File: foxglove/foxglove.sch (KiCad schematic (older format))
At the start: 50 parts, among them J1 NEIGHBOR1, J2 NEIGHBOR2, J3 Conn_02x05_Odd_Even, J4 Conn_02x05_Odd_Even, J5 Conn_01x02_Female, J7 BONUS_ROW, U1 ICE40HX8K-CT256, U2 TLV711, U3 MC4558CPT, U4 74LVC1G3157, U5 LM339, U6 ADP225, U7 DAC084S085, U8 74AHC1G04

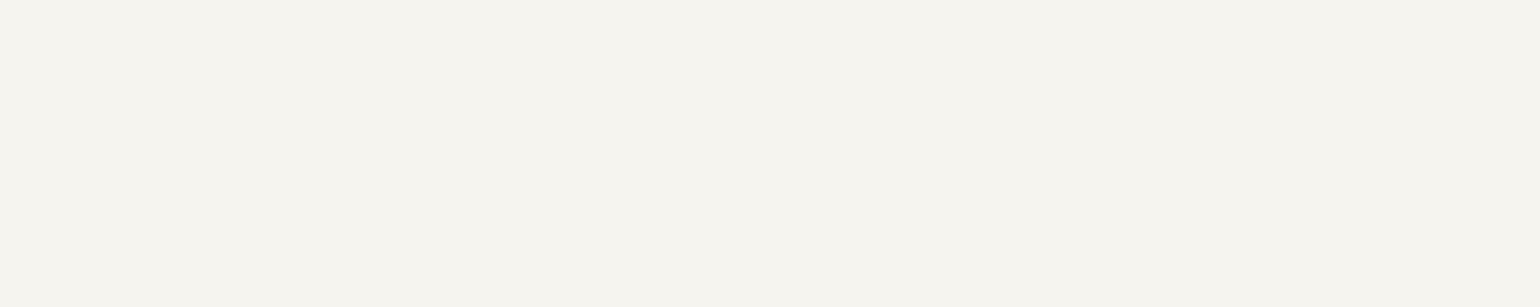
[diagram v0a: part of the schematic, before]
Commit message: Added LFE5U-12F-6BG256C to schematic
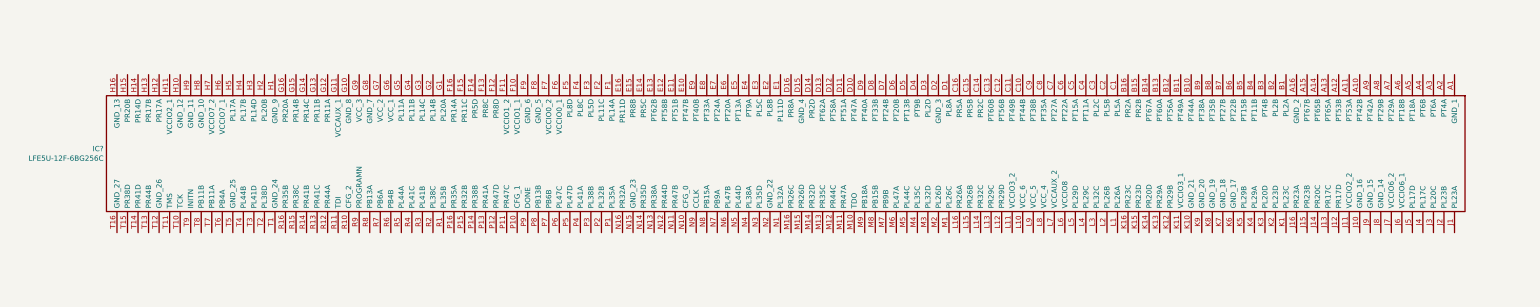
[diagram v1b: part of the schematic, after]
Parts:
- added IC?: LFE5U-12F-6BG256C, BGA256C80P16X16_1400X1400X170, symbol gsg-symbols:LFE5U-12F-6BG256C
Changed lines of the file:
@@
 Text Notes 15900 8150 0    50   ~ 0
 use LDO like \nhttps://www.diodes.com/assets/Datasheets/AP2127.pdf\ninstead
+Text Notes 11600 4200 0    50   ~ 0
+need to compare between pins?
 Wire Bus Line
 	2600 1900 4600 1900
@@
 Wire Bus Line
 	3150 6800 6450 6800
-Text Notes 11600 4200 0    50   ~ 0
-need to compare between pins?
+$Comp
+L gsg-symbols:LFE5U-12F-6BG256C IC?
+U 1 1 5CBE08F5
+P -1600 5850
+F 0 "IC?" V -896 -6977 50  0000 R CNN
+F 1 "LFE5U-12F-6BG256C" V -805 -6977 50  0000 R CNN
+F 2 "BGA256C80P16X16_1400X1400X170" H -250 5950 50  0001 L CNN
+F 3 "http://www.latticesemi.com/~/media/LatticeSemi/Documents/DataSheets/ECP5/FPGA-DS-02012.pdf?document_id=50461" H -250 5850 50  0001 L CNN
+F 4 "FPGA - Field Programmable Gate Array ECP5; 12k LUTs; 1.1V" H -250 5750 50  0001 L CNN "Description"
+F 5 "1.7" H -250 5650 50  0001 L CNN "Height"
+F 6 "Lattice" H -250 5550 50  0001 L CNN "Manufacturer_Name"
+F 7 "LFE5U-12F-6BG256C" H -250 5450 50  0001 L CNN "Manufacturer_Part_Number"
+F 8 "842-LFE5U12F6BG256C" H -250 5350 50  0001 L CNN "Mouser Part Number"
+F 9 "https://www.mouser.com/Search/Refine.aspx?Keyword=842-LFE5U12F6BG256C" H -250 5250 50  0001 L CNN "Mouser Price/Stock"
+	1    -1600 5850
+	0    1    1    0
+$EndComp
 $EndSCHEMATC

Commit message: Routed FPGA power and JTAG connections
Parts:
- removed U2: TLV711, Package_SON:WSON-6_1.5x1.5mm_P0.5mm, symbol gsg-symbols:TLV711
- added R41: 25k, gsg-modules:0402, symbol Device:R
- added R42, R43: 100k, gsg-modules:0402, symbol Device:R
- added R44: 120k, gsg-modules:0402, symbol Device:R
- added R45: 10k, gsg-modules:0402, symbol Device:R
- added R46, R47: R, gsg-modules:0402, symbol Device:R
- added R? (x4): 4.7k, gsg-modules:0402, symbol Device:R
- added U2: ADP225, Package_CSP:LFCSP-8_2x2mm_P0.5mm, symbol gsg-symbols:ADP225
- added U25: 74LVC1G53, symbol gsg-symbols:74LVC1G53
- IC1: renamed from IC?; footprint BGA256C80P16X16_1400X1400X170 -> gsg-modules:BGA256C80P16X16_1400X1400X170
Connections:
- net labels added: +1V1, ADC_pull, EN_pull, TCK, TDI, TDO, TMS
- wire segments 323 -> 415
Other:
- note removed: "keep separate direction signals"
- moved on the sheet: C8, U5

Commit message: Made FPGA connections to greatfet headers
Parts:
- added J?: Conn_02x03_Odd_Even, symbol Connector_Generic:Conn_02x03_Odd_Even
- added R? (x6): 4.7k, gsg-modules:0402, symbol Device:R
- added R?: 1k, gsg-modules:0402, symbol Device:R
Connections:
- net labels added: CCLK, CFG_0, CFG_1, CFG_2, CSSPIN, INITN, J7.02, J7.03, J7.04, J7.05, J7.06, J7.07, J7.08, J7.09, J7.10, J7.11, J7.12, J7.13, J7.14, J7.15, J7.16, J7.17, J7.18, PROGRAMN
- wire segments 415 -> 462
- no-connect marks 21 -> 1
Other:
- note added: "Do we want all banks \nto be at VCCI0x = 3.3V?"
- note added: "JTAG"
- note added: "check ordering of CFG pins\nfor default setup\nSSPI: CFG[2:0] = 001"
- note removed: "make FPGA connections \nto bonus row?"
- moved on the sheet: J1, J2, J3, J4, J7, R?

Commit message: Started routing connections to J2 and J7
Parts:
- removed C1, C3: 10uF, gsg-modules:0402, symbol Device:C
- removed C2, C4: 100nF, gsg-modules:0402, symbol Device:C
- removed R1, R4, R5: 10k, gsg-modules:0402, symbol Device:R
- removed R2: ???, gsg-modules:0402, symbol Device:R
- removed R3, R6: 100, gsg-modules:0402, symbol Device:R
- removed U1: ICE40HX8K-CT256, gsg-modules:BGA256C80P16X16_1400X1400X170, symbol gsg-symbols:ICE40HX8K-CT256
- J6: renamed from J?; footprint (none) -> gsg-modules:HEADER-2x3
- U25: footprint (none) -> Package_SO:VSSOP-8_2.3x2mm_P0.5mm
- gave numbers to parts that had none: 11
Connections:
- net labels removed: +1V2, CCLK, CDONE, CRESET
- wire segments 462 -> 349
- no-connect marks 1 -> 0
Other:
- moved on the sheet: C5, C6, C7, R41, R42, R43, R44, U2

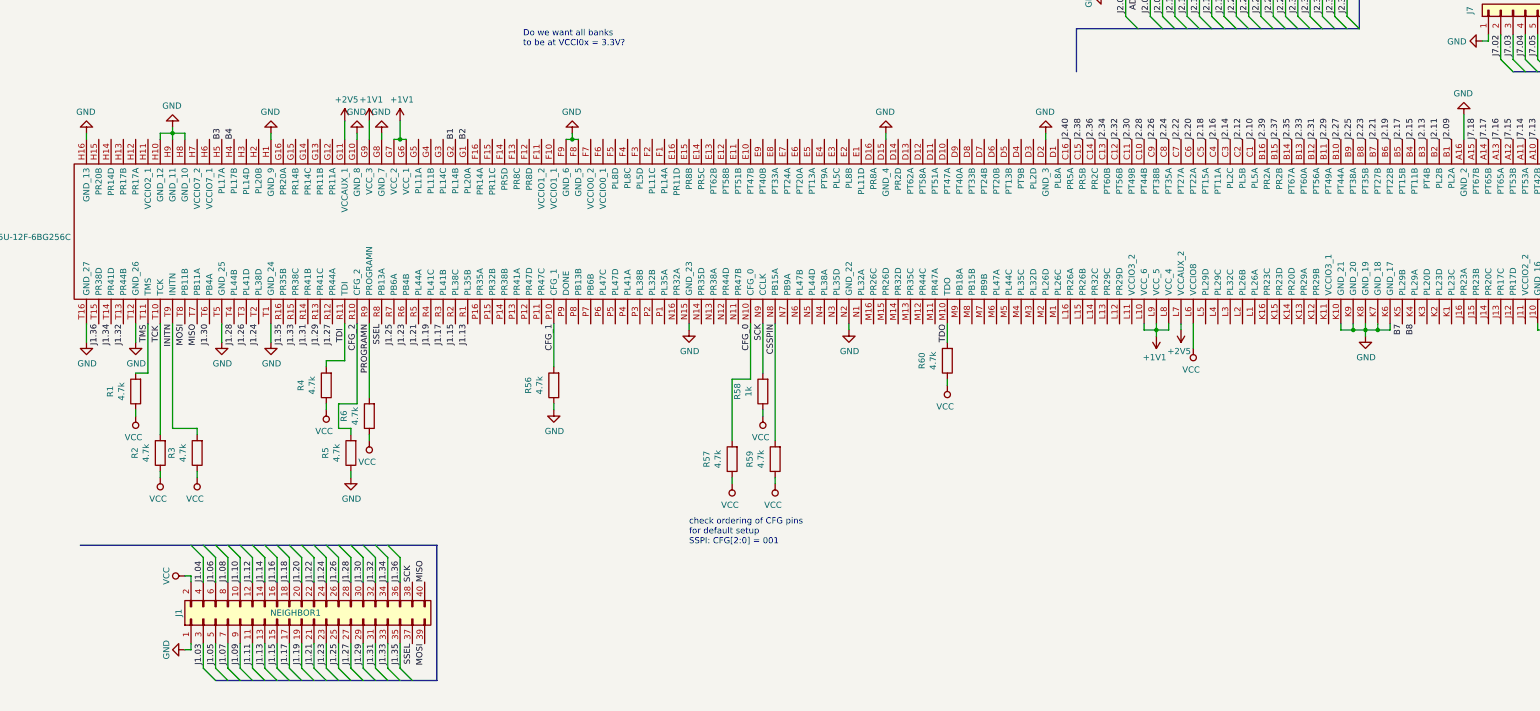
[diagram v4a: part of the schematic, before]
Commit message: Routed all greatfet headers to FPGA
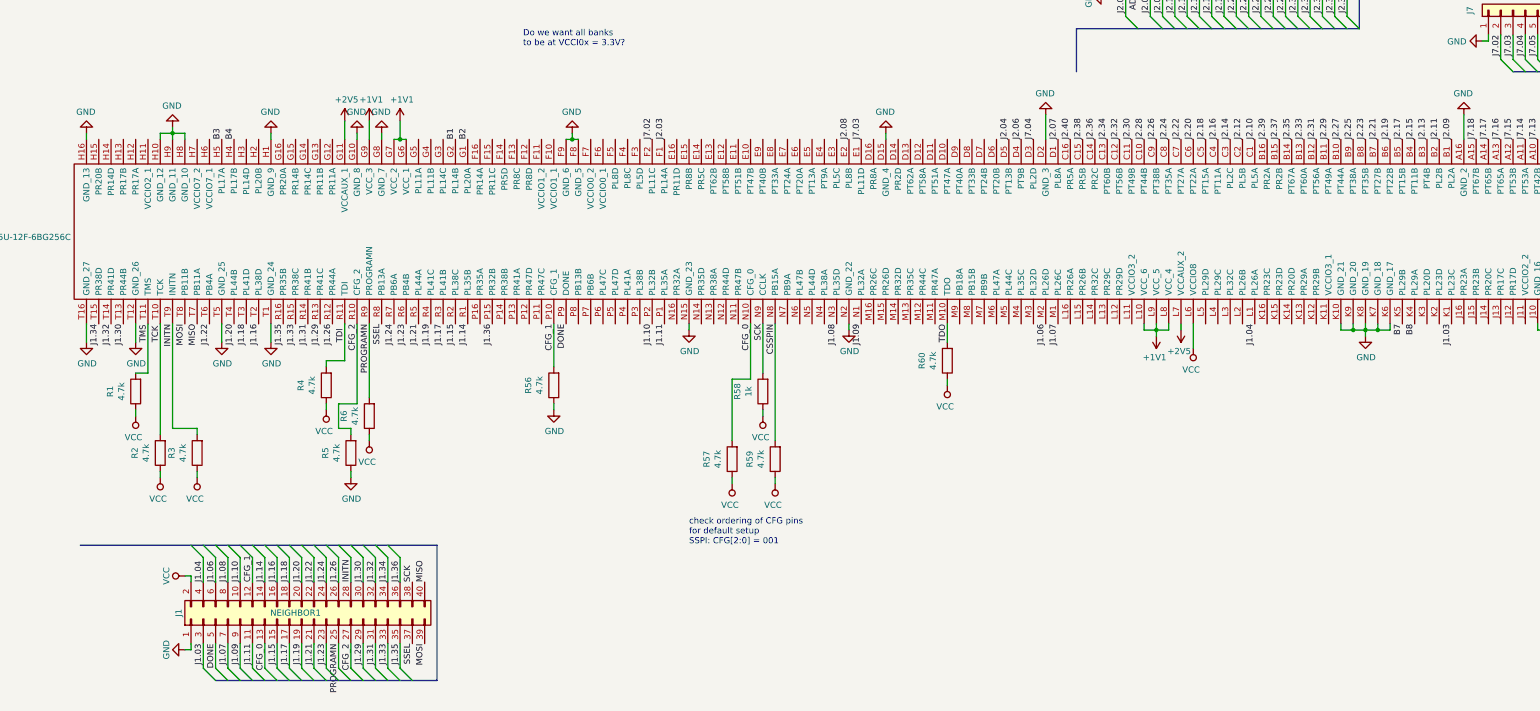
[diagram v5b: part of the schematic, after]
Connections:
- net J1.05 is gone; now on net DONE: J1.5 (Pin_5)
- net J1.12 is gone; now on net CFG_1: J1.12 (Pin_12)
- net CFG_0: now also J1.13 (Pin_13)
- net CFG_2: now also J1.27 (Pin_27)
- net INITN: now also J1.28 (Pin_28)
- net J1.03: now also IC1.K1 (PL23C)
- net J1.04: now also IC1.L1 (PL26A)
- net J1.06: now also IC1.M2 (PL26D)
- net J1.07: now also IC1.M1 (PL26C)
- net J1.08: now also IC1.N3 (PL35D)
- net J1.09: now also IC1.N1 (PL32A)
- net J1.10: now also IC1.P2 (PL32B)
- net J1.11: now also IC1.P1 (PL35A)
- net J1.14: now also IC1.R1 (PL35B)
- net J1.16: now also IC1.T2 (PL38D)
- net J1.18: now also IC1.T3 (PL41D)
- net J1.20: now also IC1.T4 (PL44B)
- net J1.22: now also IC1.T6 (PB4A)
- net J1.24: now also IC1.R7 (PB6A); no longer IC1.T2 (PL38D)
- net J1.26: now also IC1.R12 (PR44A); no longer IC1.T3 (PL41D)
- net J1.30: now also IC1.T13 (PR44B); no longer IC1.T6 (PB4A)
- net J1.32: now also IC1.T14 (PR41D); no longer IC1.T13 (PR44B)
- net J1.34: now also IC1.T15 (PR38D); no longer IC1.T14 (PR41D)
- net J1.36: now also IC1.P15 (PR32B); no longer IC1.T15 (PR38D)
- net J2.03: now also IC1.F1 (PL14A)
- net J2.04: now also IC1.D5 (PT13B)
- net J2.06: now also IC1.D4 (PT9B)
- net J2.07: now also IC1.D1 (PL8A)
- net J2.08: now also IC1.E2 (PL8B)
- net J7.02: now also IC1.F2 (PL11C)
- net J7.03: now also IC1.E1 (PL11D)
- net J7.04: now also IC1.D3 (PL2D)
- net PROGRAMN: now also J1.25 (Pin_25)
- net DONE: now reaches IC1.P9 (DONE)
- removed net J1.13: IC1.R1 (PL35B), J1.13 (Pin_13)
- removed net J1.25: IC1.R7 (PB6A), J1.25 (Pin_25)
- removed net J1.27: IC1.R12 (PR44A), J1.27 (Pin_27)
- removed net J1.28: IC1.T4 (PL44B), J1.28 (Pin_28)
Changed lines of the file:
@@
 	-13450 10000 -13500 10000
 Text Label -13250 9950 3    50   ~ 0
-J1.05
+DONE
 Text Label -13150 9950 3    50   ~ 0
 J1.07
@@
 J1.11
 Text Label -12850 9950 3    50   ~ 0
-J1.13
+CFG_0
 Text Label -12750 9950 3    50   ~ 0
 J1.15
@@
 Text Label -12350 9950 3    50   ~ 0
 J1.23
-Text Label -12250 9950 3    50   ~ 0
-J1.25
-Text Label -12150 9950 3    50   ~ 0
-J1.27
 Text Label -12050 9950 3    50   ~ 0
 J1.29
@@
 Text Label -13050 9450 1    50   ~ 0
 J1.10
-Text Label -12950 9450 1    50   ~ 0
-J1.12
 Text Label -12850 9450 1    50   ~ 0
 J1.14
@@
 Text Label -12250 9450 1    50   ~ 0
 J1.26
-Text Label -12150 9450 1    50   ~ 0
-J1.28
 Text Label -12050 9450 1    50   ~ 0
 J1.30
@@
 Entry Wire Line
 	-11850 9150 -11750 9250
-Wire Bus Line
-	-11450 10250 -11450 9150
 Wire Wire Line
 	-13350 9950 -13350 10150
@@
 L power:GND #PWR0211
 U 1 1 5D1496A8
-P -6500 5800
-F 0 "#PWR0211" H -6500 5550 50  0001 C CNN
-F 1 "GND" H -6495 5627 50  0000 C CNN
-F 2 "" H -6500 5800 50  0001 C CNN
-F 3 "" H -6500 5800 50  0001 C CNN
-	1    -6500 5800
+P -6500 5650
+F 0 "#PWR0211" H -6500 5400 50  0001 C CNN
+F 1 "GND" H -6495 5477 50  0000 C CNN
+F 2 "" H -6500 5650 50  0001 C CNN
+F 3 "" H -6500 5650 50  0001 C CNN
+	1    -6500 5650
 	-1   0    0    1
 $EndComp
-Wire Wire Line
-	-6500 5850 -6500 5800
 $Comp
 L power:GND #PWR0212
@@
 Text Label -4800 5850 1    50   ~ 0
 J2.10
-Text Label -14200 7350 3    50   ~ 0
-J1.36
 Wire Wire Line
 	-14300 7350 -14300 7500
-Text Label -14100 7350 3    50   ~ 0
+Text Label -14200 7350 3    50   ~ 0
 J1.34
-Text Label -14000 7350 3    50   ~ 0
+Text Label -14100 7350 3    50   ~ 0
 J1.32
-Text Label -13300 7350 3    50   ~ 0
-J1.30
-Text Label -13100 7350 3    50   ~ 0
-J1.28
-Text Label -13000 7350 3    50   ~ 0
-J1.26
-Text Label -12900 7350 3    50   ~ 0
-J1.24
 Wire Wire Line
 	-13200 7350 -13200 7500
@@
 J1.29
 Text Label -12300 7350 3    50   ~ 0
-J1.27
+J1.26
 Text Label -11900 7350 3    50   ~ 0
 SSEL
@@
 J1.15
 Text Label -11200 7350 3    50   ~ 0
-J1.13
+J1.14
 Text Label -11800 7350 3    50   ~ 0
-J1.25
+J1.24
 Text Label -11200 5850 1    50   ~ 0
 B2
@@
 Text Notes -10750 5100 0    50   ~ 0
 Do we want all banks \nto be at VCCI0x = 3.3V?
+Text Label -13500 7350 3    50   ~ 0
+MOSI
+Text Label -13400 7350 3    50   ~ 0
+MISO
+Text Label -12900 7350 3    50   ~ 0
+J1.16
+Text Label -13000 7350 3    50   ~ 0
+J1.18
+Text Label -13100 7350 3    50   ~ 0
+J1.20
+Text Label -13300 7350 3    50   ~ 0
+J1.22
+Text Label -12250 9950 3    50   ~ 0
+PROGRAMN
+Wire Bus Line
+	-11450 10250 -11450 9150
+Text Label -12150 9450 1    50   ~ 0
+INITN
+Text Label -12150 9950 3    50   ~ 0
+CFG_2
+Text Label -14000 7350 3    50   ~ 0
+J1.30
+Text Label -11000 7350 3    50   ~ 0
+J1.36
+Text Label -6600 5850 1    50   ~ 0
+J7.04
+Text Label -6400 5850 1    50   ~ 0
+J2.07
+Wire Wire Line
+	-6500 5650 -6500 5850
 Wire Bus Line
 	-5950 3850 -3950 3850
@@
 Wire Bus Line
 	-2700 5300 -950 5300
-Text Label -13500 7350 3    50   ~ 0
-MOSI
-Text Label -13400 7350 3    50   ~ 0
-MISO
+Text Label -8100 5850 1    50   ~ 0
+J2.08
+Text Label -8000 5850 1    50   ~ 0
+J7.03
+Text Label -6700 5850 1    50   ~ 0
+J2.06
+Text Label -6800 5850 1    50   ~ 0
+J2.04
+Text Label -9700 5850 1    50   ~ 0
+J7.02
+Text Label -9600 5850 1    50   ~ 0
+J2.03
+Text Label -12950 9450 1    50   ~ 0
+CFG_1
+Text Label -9700 7350 3    50   ~ 0
+J1.10
+Text Label -9600 7350 3    50   ~ 0
+J1.11
+Text Label -8200 7350 3    50   ~ 0
+J1.08
+Text Label -8000 7350 3    50   ~ 0
+J1.09
+Text Label -6500 7350 3    50   ~ 0
+J1.06
+Text Label -6400 7350 3    50   ~ 0
+J1.07
+Text Label -10400 7350 3    50   ~ 0
+DONE
+Text Label -4800 7350 3    50   ~ 0
+J1.04
+Text Label -3200 7350 3    50   ~ 0
+J1.03
 $EndSCHEMATC

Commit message: Changed DAC controlled LDO
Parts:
- added C?: 1uF, gsg-modules:0402, symbol Device:C
- added JP?: Jumper_3_Bridged12, symbol Jumper:Jumper_3_Bridged12
- added U?: AP2127, symbol gsg-symbols:AP2127
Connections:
- net GND: now also U?.2 (GND)
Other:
- moved on the sheet: IC1, J1, J2, J6, J7, R1, R2, R3, R4, R5, R56, R57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

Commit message: Added design notes
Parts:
- removed JP?: Jumper_3_Bridged12, symbol Jumper:Jumper_3_Bridged12
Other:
- note added: "TODO: standard JTAG header?"
- note added: "bank B: add DAC/LDO to use\nfull range of FPGA"
- note added: "https://github.com/tinyfpga/TinyFPGA-EX/tree/master/board\n"
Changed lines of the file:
@@
 	1    0    0    -1
 $EndComp
+Wire Wire Line
+	17450 7150 17450 7400
 Wire Bus Line
 	-5400 2700 -3400 2700
@@
 Wire Bus Line
 	-2150 4150 -400 4150
-Wire Wire Line
-	17450 7150 17450 7400
-$Comp
-L Jumper:Jumper_3_Bridged12 JP?
-U 1 1 5CE7E7ED
-P 18800 8050
-F 0 "JP?" H 18800 8254 50  0000 C CNN
-F 1 "Jumper_3_Bridged12" H 18800 8163 50  0000 C CNN
-F 2 "" H 18800 8050 50  0001 C CNN
-F 3 "~" H 18800 8050 50  0001 C CNN
-	1    18800 8050
-	1    0    0    -1
-$EndComp
+Text Notes -10100 9050 0    50   ~ 0
+TODO: standard JTAG header?
+Text Notes -9950 9200 0    50   ~ 0
+https://github.com/tinyfpga/TinyFPGA-EX/tree/master/board\n
+Text Notes 14700 4100 0    50   ~ 0
+bank B: add DAC/LDO to use\nfull range of FPGA
 $EndSCHEMATC

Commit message: Connected bank B to VCCIO7 pins, switched out voltage regulators
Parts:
- removed C8, C9: 0.1uF, gsg-modules:0402, symbol Device:C
- removed R46, R47: R, gsg-modules:0402, symbol Device:R
- removed U3: MC4558CPT, Package_SO:TSSOP-8_4.4x3mm_P0.65mm, symbol gsg-symbols:MC4558CPT
- removed U5: LM339, Package_SO:SOIC-14_3.9x8.7mm_P1.27mm, symbol gsg-symbols:LM339
- removed U8: 74AHC1G04, Package_TO_SOT_SMD:SOT-886, symbol gsg-symbols:74AHC1G04
- added C2: 4.7uF, symbol Device:C
- added C3: 2.7nF, symbol Device:C
- added R18, R19: 10k, gsg-modules:0402, symbol Device:R
- added R21, R22: R, symbol Device:R
- added U1: LM393, symbol gsg-symbols:LM393
- U3: renamed from U?; footprint (none) -> Package_TO_SOT_SMD:SOT-23-5
- gave numbers to parts that had none: 1
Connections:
- net +5V: now also C1.2, U3.1 (VIN), U1.8 (VCC)
- net B7: now also IC1.K2 (PL23D); no longer IC1.K5 (PL29B)
- net B8: now also IC1.K1 (PL23C); no longer IC1.K4 (PL29A)
- net COMP1: now also U1.3 (INA+)
- net COMP2: now also U1.5 (INB+)
- net COUT1: now also U1.1 (OUTA)
- net COUT2: now also U1.7 (OUTB)
- net DAC3: now also U7.4 (VOUTC), U1.2 (INA-)
- net DAC4: now also U7.5 (VOUTD), U1.6 (INB-)
- net GND: now also C1.1, C2.1, C3.2, R18.2, R21.2, R22.1, U1.4 (GND)
- net J1.03: now also IC1.K4 (PL29A); no longer IC1.K1 (PL23C)
- net J2.03: now also IC1.E6 (PT20A); no longer IC1.F1 (PL14A)
- net J2.04: now also IC1.D7 (PT24B); no longer IC1.D5 (PT13B)
- net J2.06: now also IC1.D6 (PT20B); no longer IC1.D4 (PT9B)
- net J2.07: now also IC1.D4 (PT9B); no longer IC1.D1 (PL8A)
- net J2.08: now also IC1.E5 (PT13A); no longer IC1.E2 (PL8B)
- net J2.09: now also IC1.D8 (PT33B); no longer IC1.B1 (PL2A)
- net J2.10: now also IC1.E8 (PT33A); no longer IC1.C1 (PL5A)
- net J2.11: now also IC1.D9 (PT40A); no longer IC1.B2 (PL2B)
- net J2.12: now also IC1.E9 (PT40B); no longer IC1.C2 (PL5B)
- net J2.14: now also IC1.E10 (PT47B); no longer IC1.C3 (PL2C)
- net J7.02: now also IC1.E7 (PT24A); no longer IC1.F2 (PL11C)
- net J7.03: now also IC1.E4 (PT9A); no longer IC1.E1 (PL11D)
- net J7.04: now also IC1.D5 (PT13B); no longer IC1.D3 (PL2D)
- net SSEL: now also R15.2, U7.9 (~SYNC~)
- net VCC: no longer J4.9 (Pin_9)
- net VCCA: now also U3.5 (VOUT), C2.2, C3.1, R19.2, R22.2
- net VCCA_EN: now also U3.3 (~Shutdown~)
- net VCCB: now reaches IC1.H6 (VCCIO7_1)
- net VCCB: now also IC1.H7 (VCCIO7_2), J4.9 (Pin_9)
- net at U25.6 (Y1): now also R19.1
- net at U25.7 (Y0): now also R18.1
- net at U3.4 (ADJ): now also R21.1
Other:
- note added: "1.14 <VCCIO < 3.465"
- note added: "TODO: calculate resistances,\nadd regulator for DAC2 and VCCB"
- note added: "bank 7"
- note added: "bank A: ADC, DAC, level shifter, pull-up, pull-down, comparator\nbank B: FPGA (VCCIO bank 7)"
- note added: "comparators"
- note removed: "Do we want all banks \nto be at VCCI0x = 3.3V?"
- note removed: "add another LDO\nfor DAC3 and DAC4?"
- note removed: "bank A: ADC, DAC, level shifter, pull-up, pull-down, comparator\nbank B: FPGA"
- note removed: "check digital levels\nfor comp (5V)"
- note removed: "comparator bank"
- note removed: "need to compare between pins?"
- note removed: "take LDO to header, not through mux (resistance too high)"
- moved on the sheet: J5
